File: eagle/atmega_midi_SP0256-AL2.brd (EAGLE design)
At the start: 101 x 81 mm, 44 parts, among them U1 6N138, U2 ATMEGA328P_PDIP, U3 SP0256-AL2, U4 TL072P

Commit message: added ltc6904
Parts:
- removed Q2: (no value), crystal:HC49/S
- removed R25: 470, rcl:0207/7
- removed VEL_LED: (no value), SparkFun-LED:LED5MM
- added IC1: LTC6904, linear-technology-3:DIL08
- added R5: 10, rcl:0207/7
- C14: value 27pF -> .1uF; device rcl:C025-040X050 -> rcl:C025-030X050
- C15: value 27pF -> 47p; device rcl:C025-040X050 -> rcl:C050-024X044
- moved C15 124.2 mm to (2.54, -45.7)
- moved C14 104.1 mm to (1.27, -17.8)
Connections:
- removed net N$18: R25.1, VEL_LED.A
- removed net N$20: R25.2, U2.12
- removed net N$38: C14.1, Q2.1, U3.P$28
- new net N$29: C15.2, IC1.5
- new net N$33: R5.2, U3.P$27
- net +5V: now also IC1.7, IC1.8
- net GND: now also IC1.1, U3.P$28; no longer C14.2, C15.2, VEL_LED.K
- net N$39: now also R5.1; no longer Q2.2, U3.P$27
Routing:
- net GND: track 381.0 -> 362.6 mm
- net N$39: track 16.4 -> 0.00 mm
- net N$20: track 10.6 -> 0.00 mm
- net N$33: track 0.00 -> 10.5 mm
- net N$38: track 10.1 -> 0.00 mm
- net N$18: track 4.19 -> 0.00 mm
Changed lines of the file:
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@@
 <?xml version="1.0" encoding="utf-8"?>
 <!DOCTYPE eagle SYSTEM "eagle.dtd">
-<eagle version="7.6.0">
+<eagle version="7.7.0">
 <drawing>
 <settings>
@@
 <element name="C12" library="rcl" package="C025-030X050" value="100n" x="31.75" y="44.45" rot="R270"/>
 <element name="C13" library="rcl" package="B45181A" value="1uF" x="81.534" y="50.8"/>
-<element name="C14" library="rcl" package="C025-040X050" value="27pF" x="87.63" y="40.259"/>
-<element name="C15" library="rcl" package="C025-040X050" value="27pF" x="87.63" y="44.704"/>
 <element name="C2" library="rcl" package="C025-040X050" value="27pF" x="71.12" y="24.13" rot="R180"/>
 <element name="C3" library="rcl" package="C025-030X050" value=".1uF" x="31.75" y="33.02" rot="R90"/>
@@
 <attribute name="OC_FARNELL" value="1667008" x="62.23" y="24.13" size="1.778" layer="27" rot="R180" display="off"/>
 </element>
-<element name="Q2" library="crystal" package="HC49/S" value="" x="82.296" y="42.164" rot="R90">
-<attribute name="OC_NEWARK" value="unknown" x="82.296" y="42.164" size="1.778" layer="27" rot="R90" display="off"/>
-<attribute name="MPN" value="" x="82.296" y="42.164" size="1.778" layer="27" rot="R90" display="off"/>
-<attribute name="MF" value="" x="82.296" y="42.164" size="1.778" layer="27" rot="R90" display="off"/>
-<attribute name="OC_FARNELL" value="1667008" x="82.296" y="42.164" size="1.778" layer="27" rot="R90" display="off"/>
-</element>
 <element name="R1" library="rcl" package="0207/7" value="10k" x="24.13" y="33.02" rot="R270"/>
 <element name="R10" library="rcl" package="0207/7" value="1k" x="71.12" y="10.16" rot="R270"/>
@@
 <element name="R2" library="rcl" package="0207/7" value="220" x="13.97" y="19.05" rot="R180"/>
 <element name="R24" library="rcl" package="0207/7" value="1M" x="66.294" y="19.939" rot="R180"/>
-<element name="R25" library="rcl" package="0207/7" value="470" x="76.2" y="31.75" rot="R180"/>
 <element name="R26" library="rcl" package="0207/7" value="1k" x="33.02" y="19.05"/>
 <element name="R3" library="rcl" package="0207/7" value="270" x="21.59" y="30.48" rot="R90"/>
@@
 <element name="U3" library="speech" package="DIL28-6" value="SP0256-AL2" x="60.96" y="50.8" rot="R270"/>
 <element name="U4" library="linear" package="DIL08" value="TL072P" x="48.26" y="16.51" rot="R90"/>
-<element name="VEL_LED" library="SparkFun-LED" package="LED5MM" value="" x="84.201" y="33.147" rot="R90"/>
 <element name="RESET" library="solpad" package="LSP11" value="LSP11" x="26.67" y="29.21"/>
 <element name="RESET2" library="solpad" package="LSP11" value="LSP11" x="26.67" y="24.13"/>
 <element name="C16" library="rcl" package="C025-030X050" value="100n" x="68.58" y="62.23"/>
+<element name="IC1" library="linear-technology-3" package="DIL08" value="LTC6904" x="8.89" y="73.66"/>
+<element name="C14" library="rcl" package="C025-030X050" value=".1uF" x="1.27" y="-17.78"/>
+<element name="R5" library="rcl" package="0207/7" value="10" x="3.81" y="-31.75"/>
+<element name="C15" library="rcl" package="C050-024X044" value="47p" x="2.54" y="-45.72"/>
 </elements>
 <signals>
@@
 <wire x1="67.31" y1="62.23" x2="64.64490625" y2="62.23" width="1.016" layer="16"/>
 <wire x1="64.64490625" y1="62.23" x2="61.970878125" y2="59.555971875" width="1.016" layer="16"/>
+<contactref element="IC1" pad="8"/>
+<contactref element="IC1" pad="7"/>
+<wire x1="5.08" y1="77.47" x2="7.62" y2="77.47" width="0" layer="19" extent="1-1"/>
+<wire x1="30.48" y1="53.38" x2="7.62" y2="77.47" width="0" layer="19" extent="1-1"/>
 </signal>
 <signal name="+12V">
@@
 <wire x1="48.26" y1="29.21" x2="48.26" y2="24.13" width="0.8128" layer="16"/>
 </signal>
-<signal name="N$20">
-<contactref element="U2" pad="12"/>
-<contactref element="R25" pad="2"/>
-<wire x1="63.5" y1="29.845" x2="63.5" y2="29.21" width="0.8128" layer="16"/>
-<wire x1="64.643" y1="31.75" x2="63.5" y2="29.845" width="0.8128" layer="16"/>
-<wire x1="72.39" y1="31.75" x2="64.643" y2="31.75" width="0.8128" layer="16"/>
-</signal>
 <signal name="N$10">
 <contactref element="R9" pad="2"/>
@@
 <wire x1="40.64" y1="22.86" x2="42.545" y2="18.415" width="0.8128" layer="16"/>
 </signal>
-<signal name="N$18">
-<contactref element="VEL_LED" pad="A"/>
-<contactref element="R25" pad="1"/>
-<wire x1="84.201" y1="31.877" x2="80.01" y2="31.75" width="0.8128" layer="16"/>
-</signal>
 <signal name="GND">
 <contactref element="MIDI_IN" pad="PE"/>
@@
 <contactref element="MIDI_IN" pad="PE2"/>
 <contactref element="U3" pad="P$22"/>
-<contactref element="C15" pad="2"/>
 <contactref element="C6" pad="2"/>
 <contactref element="AMT" pad="1"/>
 <contactref element="OUTPUT" pad="P$1"/>
 <contactref element="U3" pad="P$1"/>
-<contactref element="C14" pad="2"/>
-<contactref element="VEL_LED" pad="K"/>
 <contactref element="RESET2" pad="MP"/>
 <contactref element="U1" pad="5"/>
@@
 <contactref element="PWR1" pad="3"/>
 <contactref element="PWR1" pad="6"/>
-<wire x1="88.9" y1="44.704" x2="88.9" y2="40.259" width="1.016" layer="16"/>
 <wire x1="86.995" y1="59.182" x2="78.74" y2="59.182" width="1.016" layer="16"/>
 <wire x1="78.74" y1="59.182" x2="77.978" y2="58.42" width="1.016" layer="16"/>
@@
 <wire x1="86.995" y1="50.673" x2="86.995" y2="59.182" width="1.016" layer="16"/>
 <wire x1="88.9" y1="47.752" x2="86.995" y2="50.673" width="1.016" layer="16"/>
-<wire x1="88.9" y1="47.752" x2="88.9" y2="44.704" width="1.016" layer="16"/>
-<wire x1="84.201" y1="34.417" x2="88.646" y2="37.973" width="1.016" layer="16"/>
-<wire x1="88.646" y1="37.973" x2="88.9" y2="40.259" width="1.016" layer="16"/>
 <wire x1="10.16" y1="2.54" x2="7.62" y2="2.54" width="0.8128" layer="16"/>
 <wire x1="17.78" y1="2.54" x2="15.24" y2="2.54" width="0.8128" layer="16"/>
@@
 <wire x1="76.2" y1="62.23" x2="77.47" y2="60.96" width="0.8128" layer="16"/>
 <wire x1="77.47" y1="60.96" x2="77.47" y2="58.42" width="0.8128" layer="16"/>
-<wire x1="84.201" y1="34.417" x2="78.486" y2="34.417" width="0.8128" layer="16"/>
 <wire x1="52.07" y1="24.13" x2="52.07" y2="23.622" width="0.8128" layer="16"/>
 <wire x1="52.07" y1="23.622" x2="53.848" y2="21.844" width="0.8128" layer="16"/>
@@
 <wire x1="72.136" y1="39.878" x2="73.66" y2="36.83" width="0.8128" layer="16"/>
 <wire x1="73.66" y1="36.83" x2="74.7395" y2="33.7185" width="0.8128" layer="16"/>
+<contactref element="IC1" pad="1"/>
+<contactref element="U3" pad="P$28"/>
+<wire x1="80.01" y1="41.91" x2="77.47" y2="43.18" width="0.8128" layer="16"/>
+<wire x1="80.01" y1="41.91" x2="88.9" y2="47.752" width="0" layer="19" extent="16-16"/>
+<wire x1="72.136" y1="39.878" x2="77.47" y2="43.18" width="0" layer="19" extent="1-1"/>
+<wire x1="5.08" y1="69.85" x2="7.62" y2="55.88" width="0" layer="19" extent="1-1"/>
 </signal>
 <signal name="-12V">
@@
 <wire x1="80.264" y1="50.8" x2="70.485" y2="50.8" width="0.8128" layer="16"/>
 </signal>
-<signal name="N$38">
-<contactref element="Q2" pad="1"/>
-<contactref element="U3" pad="P$28"/>
-<contactref element="C14" pad="1"/>
-<wire x1="80.01" y1="41.91" x2="77.47" y2="43.18" width="0.8128" layer="16"/>
-<wire x1="82.296" y1="39.751" x2="80.01" y2="41.91" width="0.8128" layer="16"/>
-<wire x1="82.296" y1="39.751" x2="86.36" y2="40.259" width="0.8128" layer="16"/>
-</signal>
 <signal name="N$39">
-<contactref element="U3" pad="P$27"/>
-<contactref element="Q2" pad="2"/>
+<contactref element="R5" pad="1"/>
 <contactref element="C15" pad="1"/>
-<wire x1="76.2" y1="45.72" x2="74.93" y2="43.18" width="0.8128" layer="16"/>
-<wire x1="83.82" y1="45.72" x2="76.2" y2="45.72" width="0.8128" layer="16"/>
-<wire x1="83.82" y1="45.72" x2="82.296" y2="44.577" width="0.8128" layer="16"/>
-<wire x1="82.296" y1="44.577" x2="86.36" y2="44.704" width="0.8128" layer="16"/>
+<wire x1="0" y1="-31.75" x2="0" y2="-45.72" width="0" layer="19" extent="1-1"/>
 </signal>
 <signal name="N$15">
@@
 <wire x1="69.85" y1="38.1" x2="68.58" y2="36.83" width="0.8128" layer="16"/>
 </signal>
+<signal name="N$33">
+<contactref element="U3" pad="P$27"/>
+<wire x1="76.2" y1="45.72" x2="74.93" y2="43.18" width="0.8128" layer="16"/>
+<wire x1="83.82" y1="45.72" x2="76.2" y2="45.72" width="0.8128" layer="16"/>
+<contactref element="R5" pad="2"/>
+<wire x1="7.62" y1="-31.75" x2="74.93" y2="43.18" width="0" layer="19" extent="1-1"/>
+</signal>
+<signal name="N$29">
+<contactref element="IC1" pad="5"/>
+<contactref element="C15" pad="2"/>
+<wire x1="5.08" y1="-45.72" x2="12.7" y2="77.47" width="0" layer="19" extent="1-1"/>
+</signal>
 </signals>

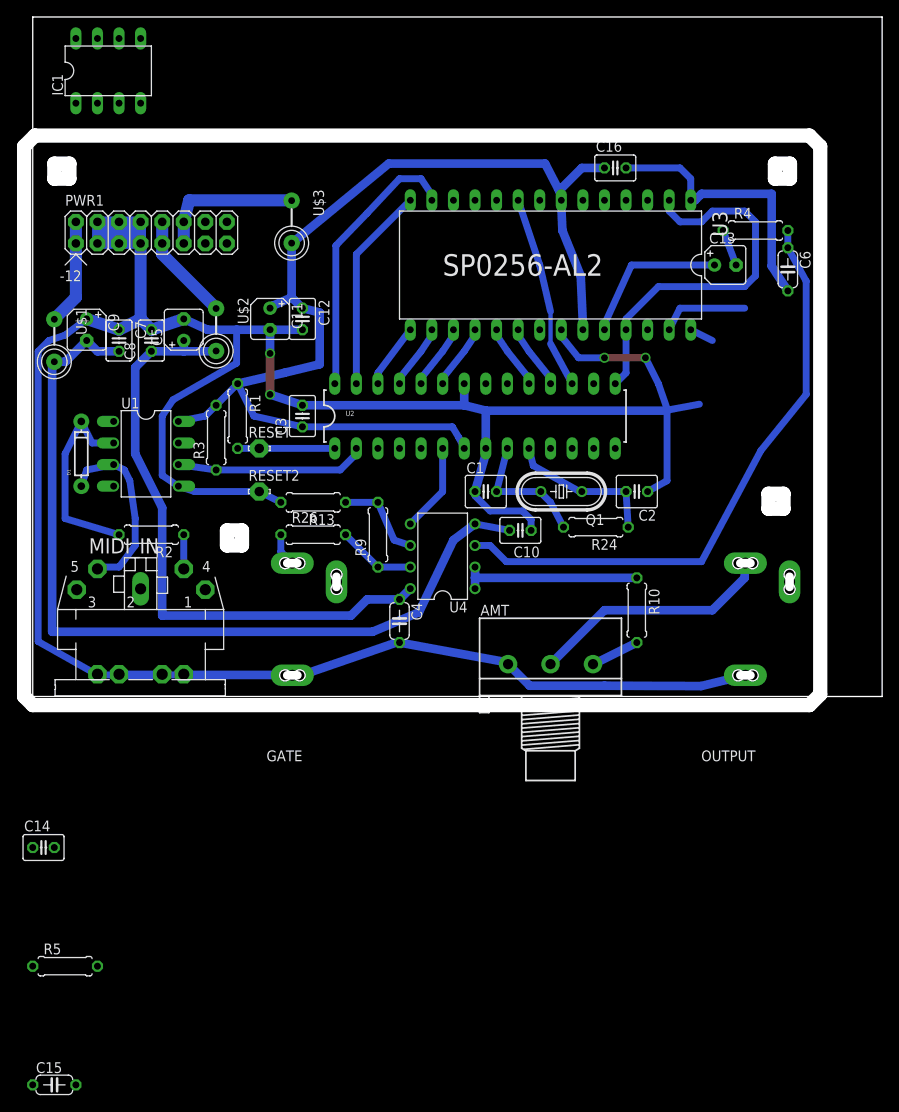
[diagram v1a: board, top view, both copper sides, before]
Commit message: renamed arduino code file and new board taking shape
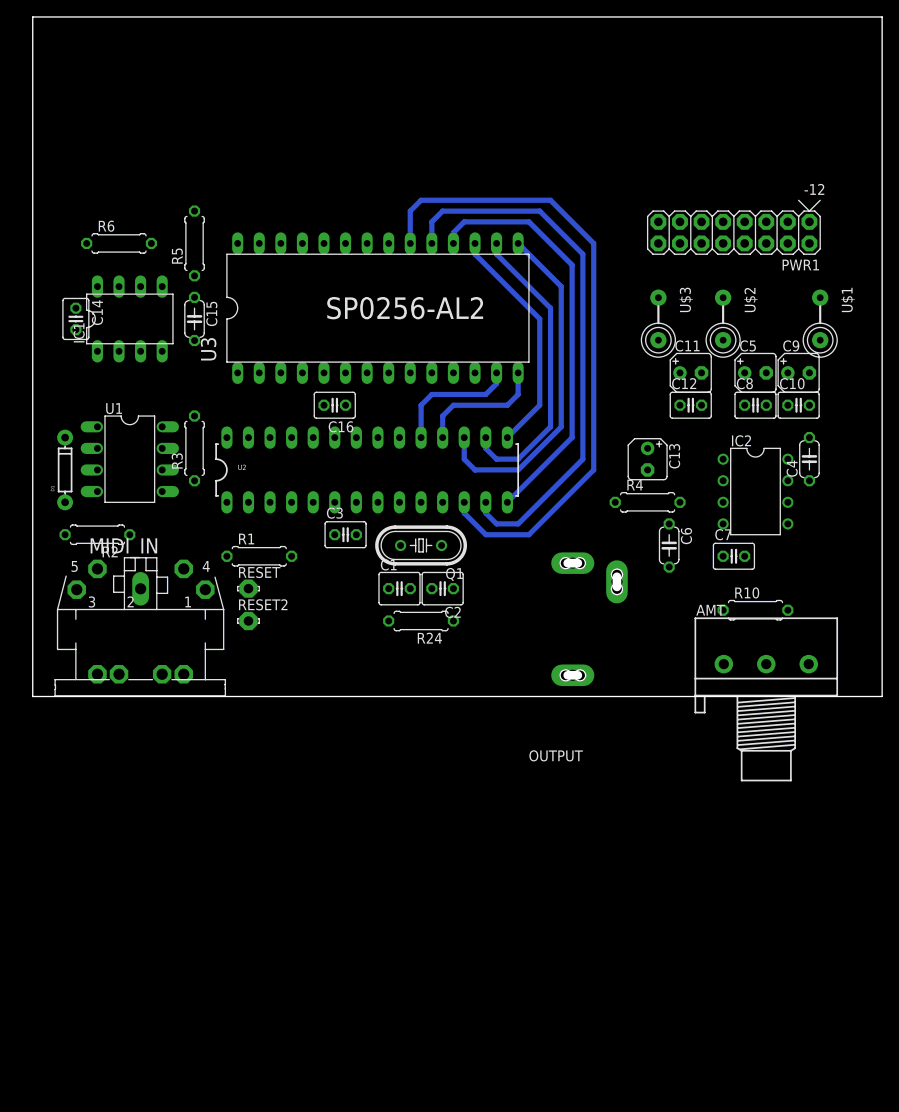
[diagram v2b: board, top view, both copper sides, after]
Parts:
- removed GATE: AUDIO-JACK, erthenvar:ERTHENVAR-JACK-90DEG
- removed R13, R26: 1k, rcl:0207/7
- removed R9: 1k5, rcl:0207/7
- removed U4: TL072P, linear:DIL08
- added IC2: TL071P, linear:DIL08
- added R6: 10k, rcl:0207/7
- moved C15 91.7 mm to (19.1, 44.5), turned to 270 degrees
- moved U$1 90.2 mm to (92.7, 44.5)
- moved R5 86.4 mm to (19.1, 53.3), turned to 90 degrees
- moved C9 84.0 mm to (90.2, 38.1), turned to 0 degrees
- moved C7 76.7 mm to (82.5, 16.5), turned to 0 degrees
- moved PWR1 73.7 mm to (85.1, 54.6), turned to 180 degrees
- moved C8 71.5 mm to (85.1, 34.3), turned to 0 degrees
- moved C5 67.5 mm to (85.1, 38.1), turned to 0 degrees
- moved C14 62.3 mm to (5.08, 44.5), turned to 270 degrees
- moved U$2 59.7 mm to (81.3, 44.5)
- moved C4 51.9 mm to (91.4, 27.9), turned to 90 degrees
- moved C11 49.9 mm to (77.5, 38.1), turned to 0 degrees
- moved C12 46.8 mm to (77.5, 34.3), turned to 0 degrees
- moved U$3 44.7 mm to (73.7, 44.5)
- moved C16 43.3 mm to (35.6, 34.3), turned to 180 degrees
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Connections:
- removed net N$19: U2.23, U3.P$18
- removed net N$21: U2.24, U3.P$17
- removed net N$22: U2.6, U4.5
- removed net N$23: U2.25, U3.P$16
- removed net N$24: U2.26, U3.P$15
- removed net N$25: U2.27, U3.P$14
- removed net N$26: U2.28, U3.P$13
- removed net N$27: U2.19, U3.P$19
- removed net N$31: GATE.P$3, R26.1
- new net A0: U2.14, U3.P$18
- new net A1: U2.15, U3.P$17
- new net A2: U2.16, U3.P$16
- new net A3: U2.17, U3.P$15
- new net A4: U2.18, U3.P$14
- new net A5: U2.19, U3.P$13
- new net N$18: IC1.2, U2.27
- net +12V: now also IC2.7; no longer U4.8
- net +5V: now also C14.1
- net -12V: now also IC2.4; no longer U4.4
- net GND: now also C14.2, R6.1; no longer GATE.P$1, R13.2
- net N$1: now also U2.26; no longer U2.15
- net N$10: now also U2.12, U3.P$20; no longer R13.1, R9.2, U4.6
- net N$12: now also IC2.2, IC2.6; no longer U4.1, U4.2
- net N$15: now also IC1.3, U2.28; no longer U2.18, U3.P$20
- net N$16: now also U2.13, U3.P$19; no longer R26.2, R9.1, U4.7
- net N$28: now also U2.23; no longer U2.17
- net N$39: now also R6.2
- net N$6: now also IC2.3; no longer U4.3
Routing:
- net GND: track 362.6 -> 0.00 mm, vias 4 -> 0
- net +5V: track 129.3 -> 0.00 mm
- net -12V: track 101.6 -> 0.00 mm
- net +12V: track 72.1 -> 0.00 mm
- net N$6: track 70.6 -> 0.00 mm
- net N$10: track 10.7 -> 75.4 mm
- net N$16: track 9.20 -> 63.5 mm
- net A0: track 0.00 -> 49.0 mm
- net N$1: track 44.8 -> 0.00 mm
- net A3: track 0.00 -> 40.3 mm
- net A2: track 0.00 -> 35.2 mm
- net N$26: track 32.6 -> 0.00 mm
- net N$13: track 28.8 -> 0.00 mm
- net A1: track 0.00 -> 27.6 mm
- net N$25: track 24.2 -> 0.00 mm
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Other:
- board size 101 x 81 mm -> 100 x 80 mm

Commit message: routed and stub code for pitch oscillator
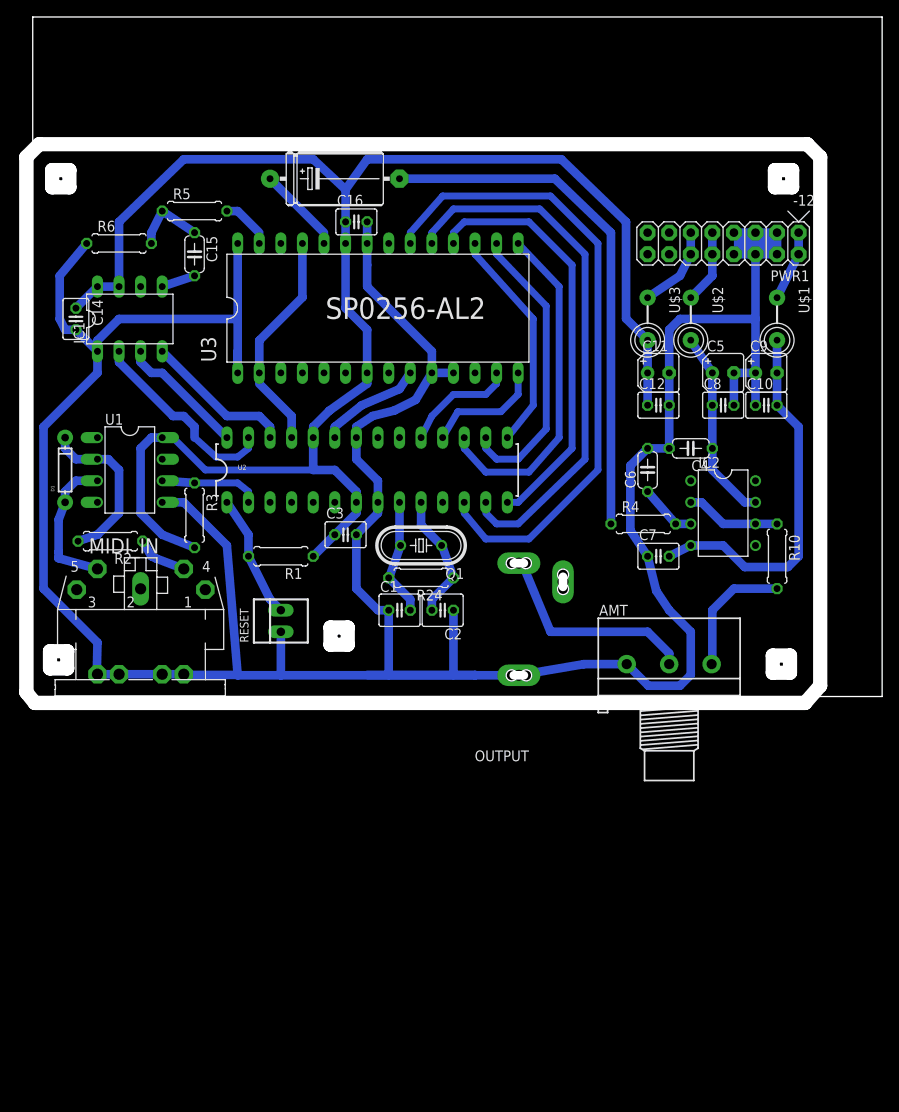
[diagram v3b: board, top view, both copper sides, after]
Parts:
- removed RESET2: LSP11, solpad:LSP11
- C13: device rcl:B45181A -> rcl:E15-6
- RESET: value LSP11 -> 22-23-2021; device solpad:LSP11 -> con-molex:22-23-2021
- moved C13 49.5 mm to (35.6, 61.0), turned to 0 degrees
- moved C16 21.7 mm to (38.1, 55.9), turned to 0 degrees
- moved C4 14.0 mm to (77.5, 29.2), turned to 180 degrees
- moved AMT 11.4 mm to (74.9, 3.81)
- moved C6 9.25 mm to (72.4, 26.7), turned to 90 degrees
- moved C7 8.89 mm to (73.7, 16.5)
- moved R3 7.87 mm to (19.1, 21.3), turned to 270 degrees
- moved C15 7.62 mm to (19.1, 52.1)
- moved R10 6.84 mm to (87.6, 16.5), turned to 270 degrees
- moved OUTPUT 6.35 mm to (62.2, 0.00)
- moved RESET 5.39 mm to (29.2, 8.89), turned to 90 degrees
- moved R24 5.08 mm to (45.7, 14.0)
- moved U$1 5.08 mm to (87.6, 44.5)
- moved IC2 4.58 mm to (81.3, 21.6)
- moved C10 3.81 mm to (86.4, 34.3)
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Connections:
- new net N$19: IC1.4, U2.26
- net +5V: now also U2.24
- net GND: now also RESET.1, U3.P$10, U3.P$11; no longer RESET2.MP
- net N$1: now also U2.25; no longer U2.26
- net N$43: now also RESET.2; no longer RESET.MP
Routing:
- net GND: track 0.00 -> 385.9 mm
- net +5V: track 0.00 -> 196.0 mm
- net N$32: track 0.00 -> 61.7 mm
- net -12V: track 0.00 -> 43.6 mm
- net N$1: track 0.00 -> 26.5 mm
- net N$13: track 0.00 -> 25.4 mm
- net N$18: track 0.00 -> 23.4 mm
- net +12V: track 0.00 -> 22.8 mm
- net N$7: track 0.00 -> 19.8 mm
- net N$19: track 0.00 -> 17.7 mm
- net N$3: track 0.00 -> 17.1 mm
- net N$5: track 0.00 -> 15.2 mm
- net N$15: track 0.00 -> 15.1 mm
- net N$9: track 0.00 -> 15.1 mm
- net N$43: track 0.00 -> 14.6 mm
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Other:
- board size 100 x 80 mm -> 100.8 x 80.8 mm
